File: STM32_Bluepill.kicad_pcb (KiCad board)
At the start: 2 copper layers, 41 x 31 mm, 32 parts, among them J1 USB_B_Micro, J2 Conn_01x04_Male, J3 Conn_01x04_Male, J4 Conn_01x04_Male, U1 STM32F103C8T6, U2 AMS1117-3.3, Y1 16MHz

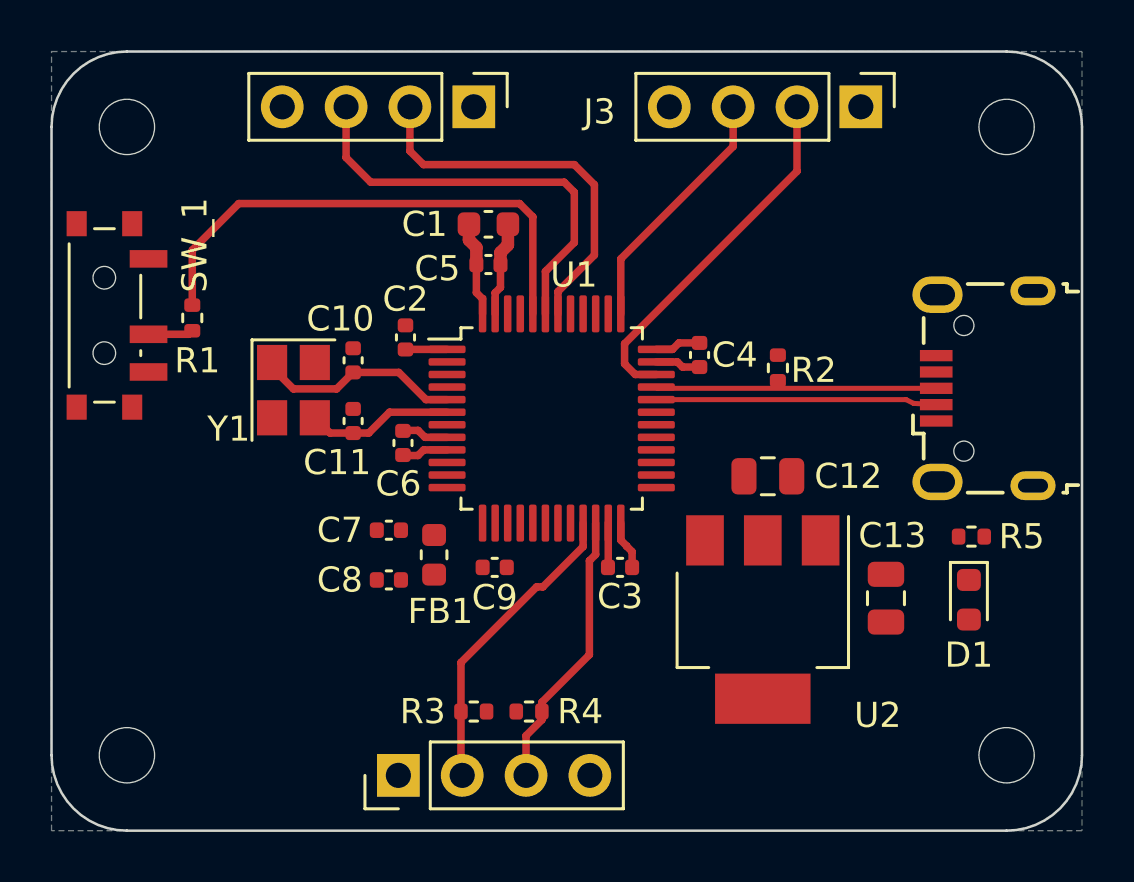
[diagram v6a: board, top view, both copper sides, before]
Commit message: Routing: Route PWR and GND
	- Use 0.5 mm tracks for these
	- Create fills for grouped GND or PWR
	- Move some things around to accommodate
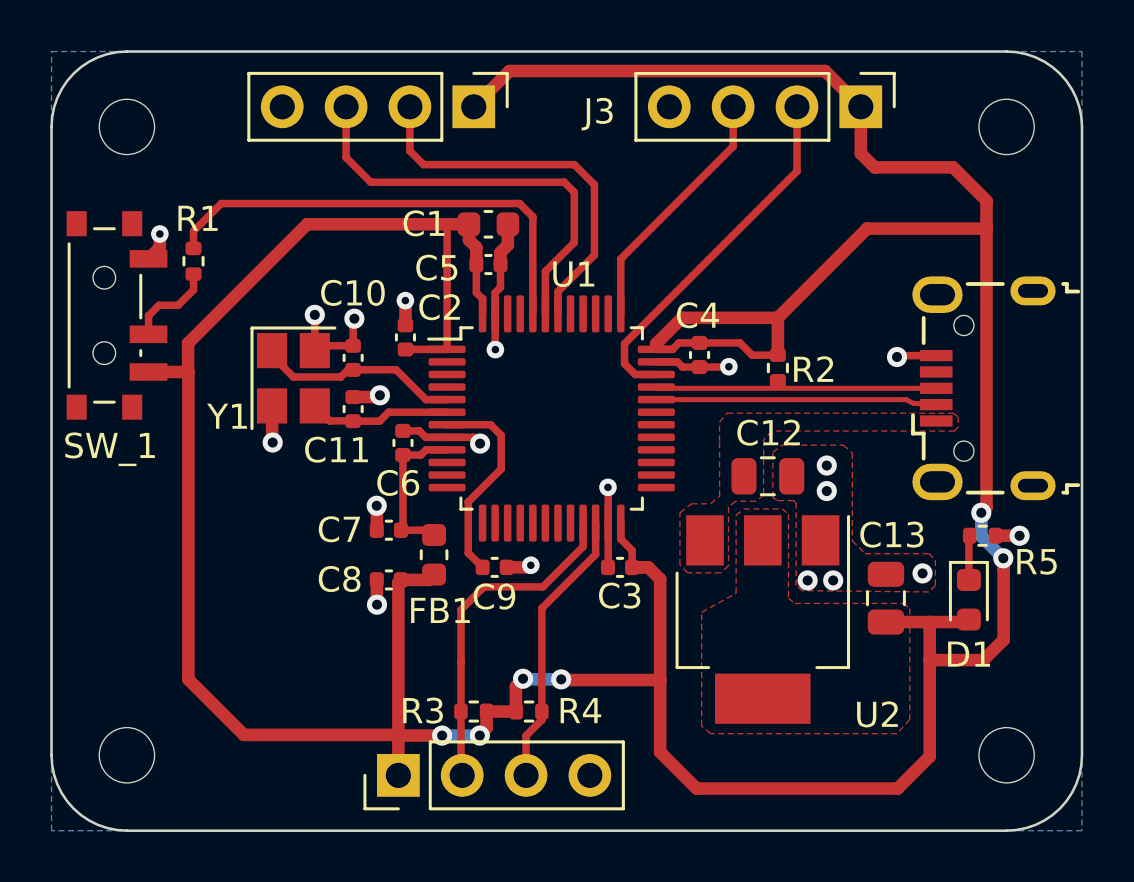
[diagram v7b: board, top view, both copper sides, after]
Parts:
- moved R1 2.26 mm to (165.0, 85.3)
- moved C11 0.47 mm to (171.4, 91.2)
- moved Y1 0.47 mm to (169.0, 90.0)
- moved R5 0.44 mm to (196.4, 96.3), turned to 0 degrees
- moved C10 0.10 mm to (171.4, 89.2)
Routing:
- net +3.3V: track 9.25 -> 167.4 mm, vias 0 -> 6
- net GND: track 9.25 -> 29.0 mm, vias 0 -> 20
- net /NRST: track 0.00 -> 8.36 mm
- net +3.3VA: track 1.88 -> 6.26 mm
- net /BOOT0: track 20.6 -> 18.7 mm
- net /SW_BOOT0: track 1.80 -> 3.58 mm
- net /PWR_LED_K: track 0.00 -> 1.77 mm
- net /I2C2_SCL: track 12.2 -> 13.4 mm
- added copper zone on F.Cu, net +3.3V
- added copper zone on F.Cu, net GND
- added copper zone on F.Cu, net VBUS

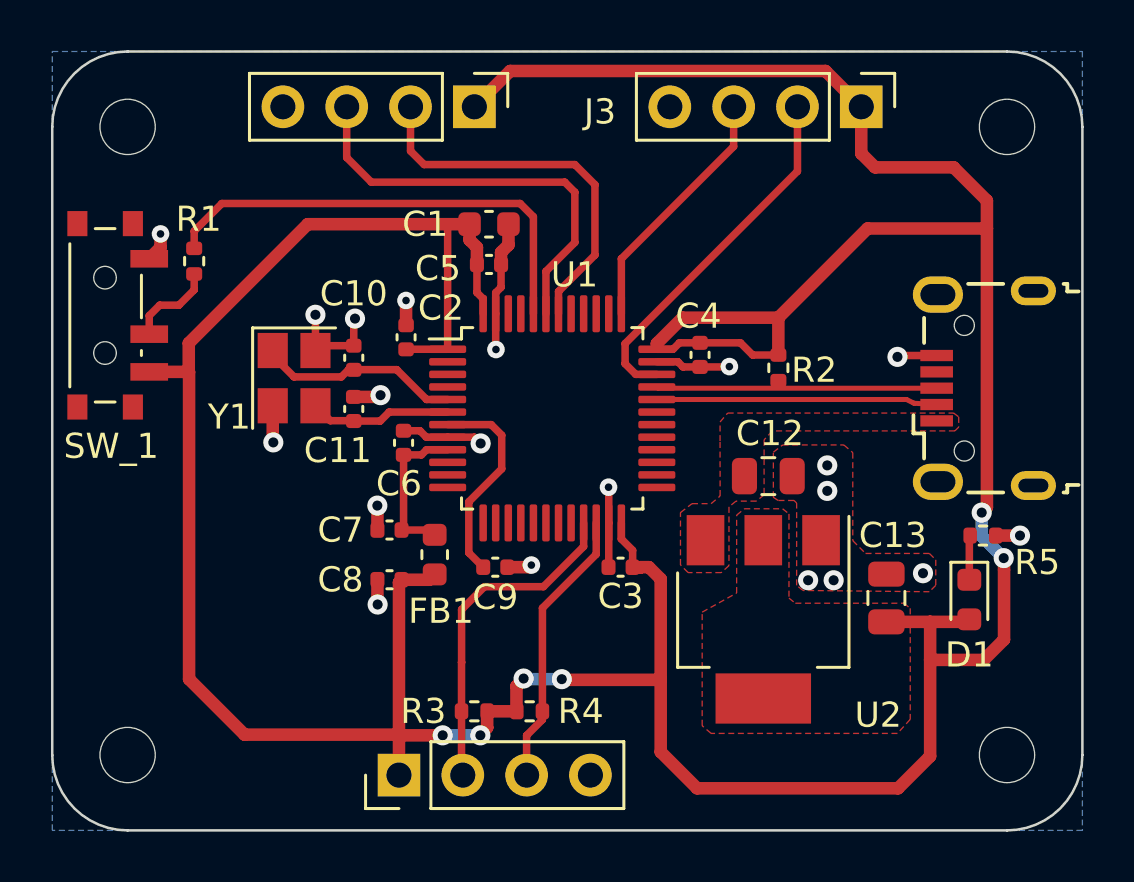
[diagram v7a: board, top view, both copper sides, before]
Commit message: Silkscreen: Put markings to indicate pin 1 on components + run DRC
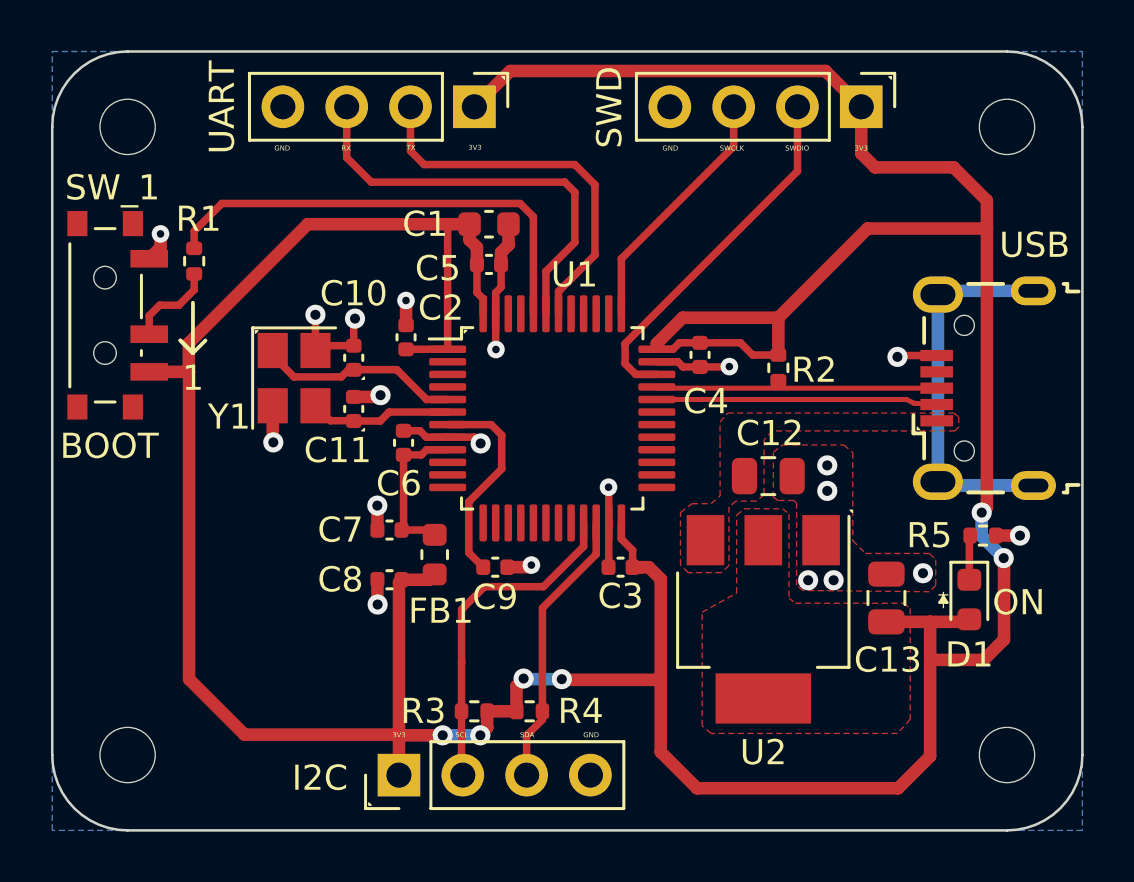
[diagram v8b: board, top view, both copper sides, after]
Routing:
- net unconnected-(J1-Pad6): track 0.00 -> 15.2 mm
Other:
- board text added: "1"
- board text added: "3V3"
- board text added: "BOOT"
- board text added: "GND"
- board text added: "I2C"
- board text added: "ON"
- board text added: "RX"
- board text added: "SCL"
- board text added: "SDA"
- board text added: "SWCLK"
- board text added: "SWD"
- board text added: "SWDIO"
- board text added: "TX"
- board text added: "UART"
- board text added: "USB"
